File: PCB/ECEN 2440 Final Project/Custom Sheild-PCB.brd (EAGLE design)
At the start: 100 x 80 mm, 4 parts

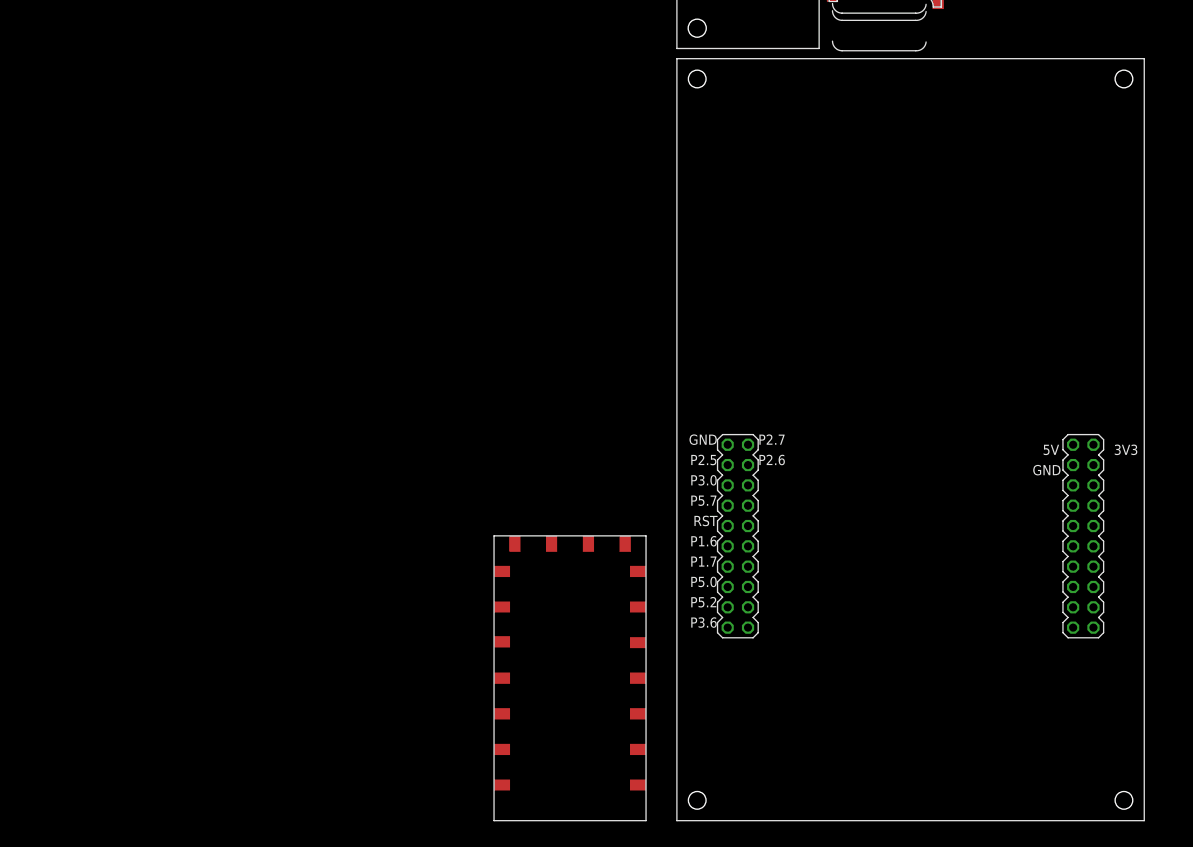
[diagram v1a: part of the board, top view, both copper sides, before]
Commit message: made a couple connections
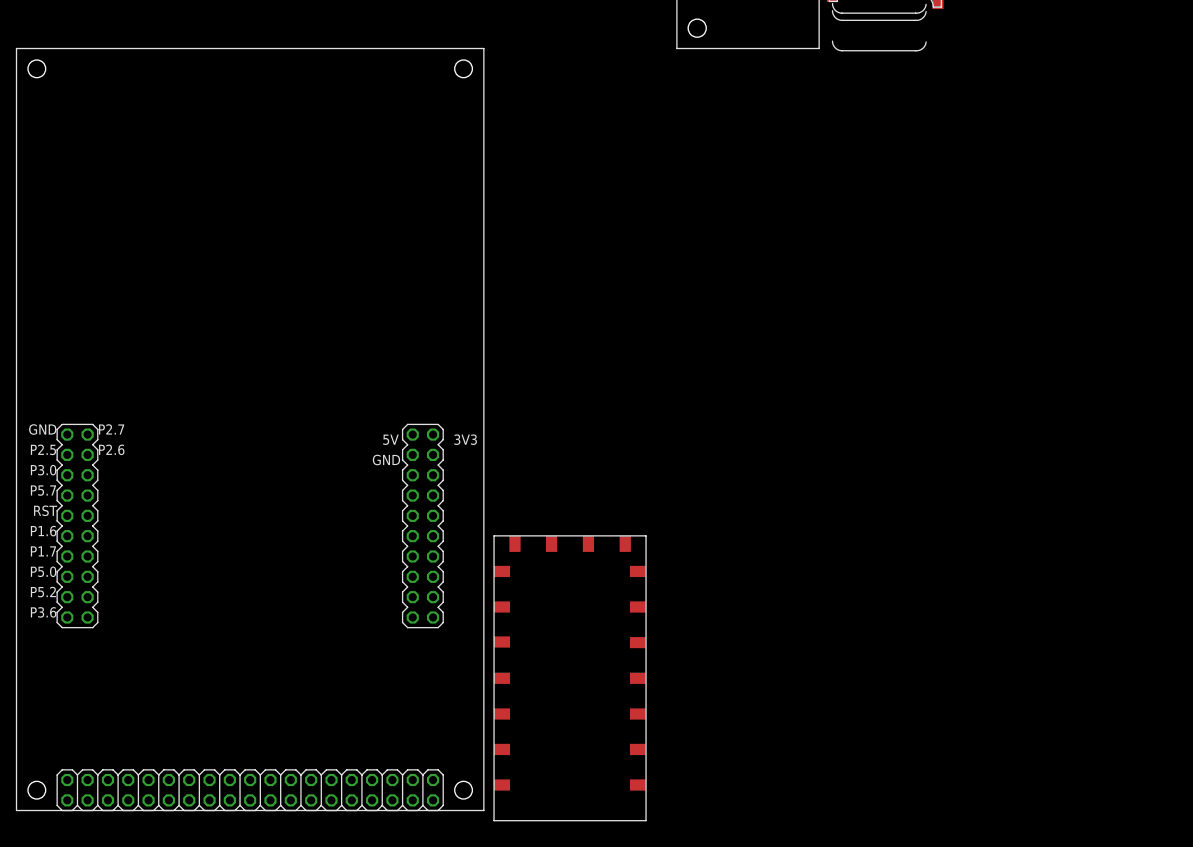
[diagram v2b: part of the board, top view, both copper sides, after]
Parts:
- moved U$3 82.6 mm to (-154.9, 2.54)
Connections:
- new net 1: U$3.GND1
- new net 29: U$3.GND2
- net GND1: no longer U$3.GND1, U$3.GND2
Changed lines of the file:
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@@
 <attribute name="NAME" x="-74.3712" y="114.3762" size="1.27" layer="25" ratio="10" rot="R270"/>
 </element>
-<element name="U$3" library="Custom Library" package="MSP432" value="MSP432" x="-72.39" y="1.27" smashed="yes"/>
 <element name="U$4" library="Custom Library" package="RADIO" value="RADIO" x="-95.25" y="1.27" smashed="yes"/>
+<element name="U$3" library="Custom Library" package="MSP432" value="MSP432" x="-154.94" y="2.54" smashed="yes">
+<attribute name="VALUE" x="-149.86" y="0.635" size="1.27" layer="27"/>
+</element>
 </elements>
 <signals>
-<signal name="30">
-<contactref element="U$3" pad="5V"/>
-</signal>
 <signal name="GND1">
-<contactref element="U$3" pad="GND1"/>
 <contactref element="U$2" pad="GND"/>
 <contactref element="U$1" pad="MT1"/>
@@
 <contactref element="U$4" pad="GND1"/>
 <contactref element="U$4" pad="GND"/>
-<contactref element="U$3" pad="GND2"/>
 <wire x1="-52.94" y1="104.57" x2="-39.74" y2="103.67" width="0" layer="19" extent="1-1"/>
 <wire x1="-69.85" y1="105.41" x2="-52.94" y2="104.57" width="0" layer="19" extent="1-1"/>
-<wire x1="-66.04" y1="48.26" x2="-69.85" y2="105.41" width="0" layer="19" extent="1-1"/>
-<wire x1="-83.45" y1="35.87" x2="-66.04" y2="48.26" width="0" layer="19" extent="1-1"/>
+<wire x1="-83.45" y1="35.87" x2="-69.85" y2="105.41" width="0" layer="19" extent="1-1"/>
 <wire x1="-88.05" y1="35.87" x2="-83.45" y2="35.87" width="0" layer="19" extent="1-1"/>
-<wire x1="-22.86" y1="45.72" x2="-66.04" y2="48.26" width="0" layer="19" extent="1-1"/>
 </signal>
 <signal name="N$1">
+<contactref element="U$2" pad="SDA"/>
 <contactref element="U$3" pad="P1.6"/>
-<contactref element="U$2" pad="SDA"/>
-<wire x1="-66.04" y1="35.56" x2="-69.85" y2="107.95" width="0" layer="19" extent="1-1"/>
+<wire x1="-69.85" y1="107.95" x2="-148.59" y2="36.83" width="0" layer="19" extent="1-1"/>
 </signal>
 <signal name="N$2">
+<contactref element="U$2" pad="SCL"/>
 <contactref element="U$3" pad="P1.7"/>
-<contactref element="U$2" pad="SCL"/>
-<wire x1="-66.04" y1="33.02" x2="-69.85" y2="110.49" width="0" layer="19" extent="1-1"/>
+<wire x1="-69.85" y1="110.49" x2="-148.59" y2="34.29" width="0" layer="19" extent="1-1"/>
 </signal>
 <signal name="N$3">
-<contactref element="U$3" pad="3V3"/>
 <contactref element="U$4" pad="VBAT"/>
 <contactref element="U$2" pad="3V3"/>
-<wire x1="-20.32" y1="48.26" x2="-92.65" y2="35.87" width="0" layer="19" extent="1-1"/>
-<wire x1="-69.85" y1="113.03" x2="-92.65" y2="35.87" width="0" layer="19" extent="1-1"/>
+<contactref element="U$3" pad="3V3"/>
+<wire x1="-102.87" y1="49.53" x2="-92.65" y2="35.87" width="0" layer="19" extent="1-1"/>
+<wire x1="-69.85" y1="113.03" x2="-102.87" y2="49.53" width="0" layer="19" extent="1-1"/>
 </signal>
 <signal name="RX_RADIO">
 <contactref element="U$4" pad="RXD"/>
 <contactref element="U$3" pad="P3.3"/>
-<wire x1="-20.32" y1="40.64" x2="-77.25" y2="14.62" width="0" layer="19" extent="1-1"/>
+<wire x1="-102.87" y1="41.91" x2="-77.25" y2="14.62" width="0" layer="19" extent="1-1"/>
 </signal>
 <signal name="TX_RADIO">
 <contactref element="U$4" pad="TXD"/>
 <contactref element="U$3" pad="P3.2"/>
-<wire x1="-20.32" y1="43.18" x2="-77.25" y2="10.17" width="0" layer="19" extent="1-1"/>
+<wire x1="-102.87" y1="44.45" x2="-77.25" y2="10.17" width="0" layer="19" extent="1-1"/>
 </signal>
 <signal name="N$4">
@@
 <contactref element="U$1" pad="5"/>
 </signal>
+<signal name="1">
+<contactref element="U$3" pad="GND1"/>
+</signal>
+<signal name="29">
+<contactref element="U$3" pad="GND2"/>
+</signal>
+<signal name="30">
+<contactref element="U$3" pad="5V"/>
+</signal>
 </signals>

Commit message: PDR schematic and board
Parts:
- added BATTERY: (no value), pinhead:1X02
- added C1, C2, C3: (no value), rcl:C0805
- added R1, R2, R3: (no value), rcl:R0805
- added SJ1, SJ2: (no value), jumper:SJ_2W
- added TEENSY: (no value), pinhead:1X04
- added U$6: LFCN-160+, Custom Library:LFCN-160+
- added U1: V_REG_NCP50X, SparkFun-IC-Power:DPAK-5
- added X1: (no value), adafruit:SMA_EDGELAUNCH
- moved U$3 156.2 mm to (1.27, 1.27)
- moved U$4 150.0 mm to (40.6, 64.8), turned to 90 degrees
- moved U$1 142.9 mm to (52.1, 21.6), turned to 270 degrees
- moved U$2 113.5 mm to (19.1, 30.5)
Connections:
- net N$1 renamed ALT_SDA
- net N$2 renamed ALT_SCL
- removed net 1: U$3.GND1
- removed net GND1: U$1.MT1, U$1.MT2, U$2.GND, U$4.GND, U$4.GND1
- new net +3V3: SJ2.2, TEENSY.4, U$1.4, U$2.3V3, U$3.3V3, U$4.VBAT
- new net AUDIO_PTT: U$3.P2.3, U$4.PTT
- new net AUDIO_PWM: R1.1, U$3.P2.4
- new net CD1: U$1.CD1, U$3.10.4
- new net GND: C1.2, C2.2, C3.2, TEENSY.1, U$1.6, U$1.MT1, U$1.MT2, U$2.GND, U$3.GND1, U$3.GND10, U$3.GND11, U$4.GND, U$4.GND1, U$6.GND1, U$6.GND2, U$6.P$1, U$6.P$2, X1.GND@1, X1.GND@2, X1.GND@3, X1.GND@4
- new net N$1: U$4.ANT, U$6.RF-IN
- new net N$2: C1.1, R1.2, R2.1
- new net N$6: U$6.RF-OUT, X1.P
- new net N$7: SJ1.1, U1.VIN
- new net N$8: SJ2.3, U1.VOUT
- new net SD_CLK: U$1.5, U$3.10.1
- new net SD_CS_SPI: U$1.2, U$3.10.0
- new net SD_MISO: U$1.7, U$3.10.2
- new net SD_MOSI: U$1.3, U$3.10.3
- new net TEENSY_RX: TEENSY.2, U$3.9.7
- new net TEENSY_TX: TEENSY.3, U$3.9.6
- new net VCC: BATTERY.2, SJ1.2
- new net VSS: BATTERY.1
- net N$3: now also U$1.CD2; no longer U$2.3V3, U$3.3V3, U$4.VBAT
- net N$4: now also C2.1, R2.2, R3.1; no longer U$1.2
- net N$5: now also C3.1, R3.2, U$4.MIC_IN; no longer U$1.5
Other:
- board size 100 x 80 mm -> 63.2 x 97.8 mm
- board text added: "LONG-SIDE PINS"
- board text added: "SHORT-SIDE PINS"

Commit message: Final board and schematic
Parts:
- added SD_BREAKOUT: (no value), pinhead:1X07
- moved BATTERY 52.1 mm to (57.1, 10.2)
- moved SJ1 48.5 mm to (57.1, 17.8)
- moved TEENSY 35.6 mm to (21.6, 15.2), turned to 270 degrees
- moved U1 33.1 mm to (48.3, 11.4), turned to 270 degrees
- moved U$1 33.0 mm to (19.1, 21.6)
- moved SJ2 12.8 mm to (35.6, 12.7)
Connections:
- removed net N$3: U$1.CD2
- net +3V3: now also SD_BREAKOUT.6
- net CD1: now also SD_BREAKOUT.1
- net GND: now also SD_BREAKOUT.7
- net SD_CLK: now also SD_BREAKOUT.4
- net SD_CS_SPI: now also SD_BREAKOUT.5
- net SD_MISO: now also SD_BREAKOUT.2
- net SD_MOSI: now also SD_BREAKOUT.3

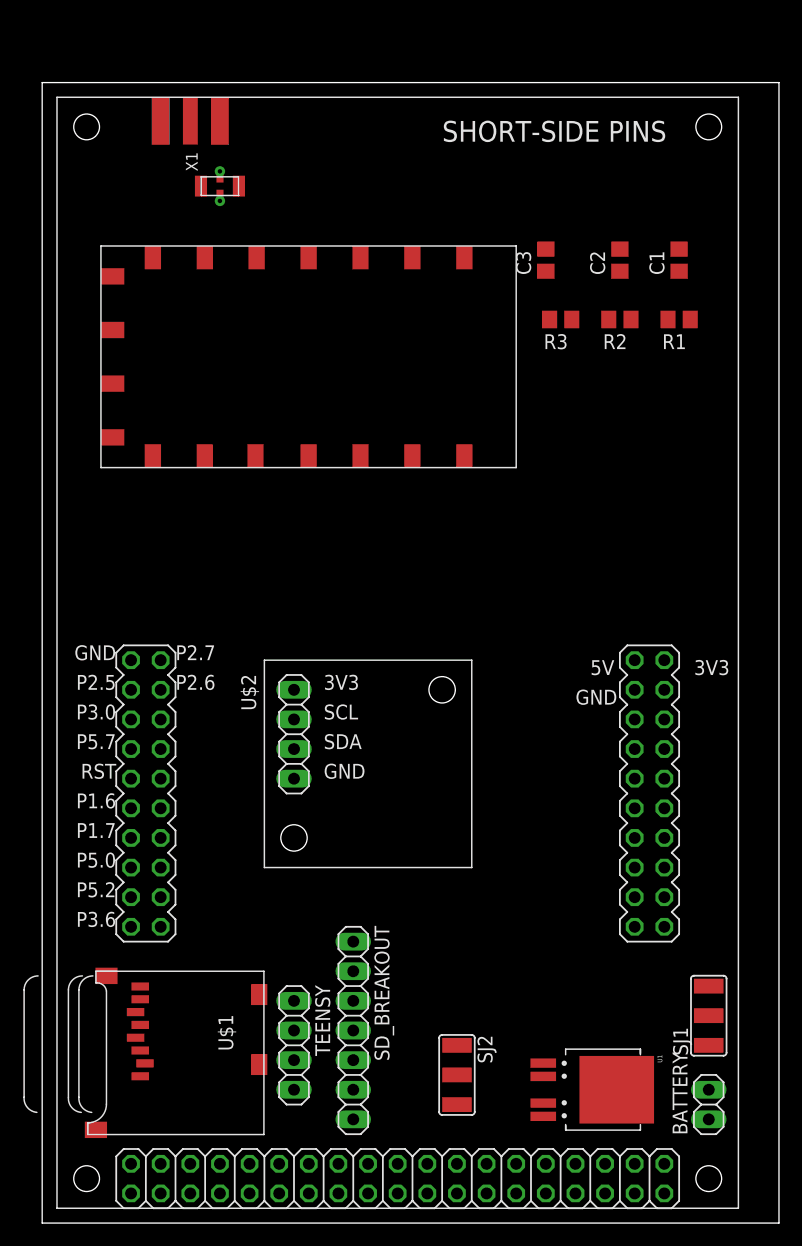
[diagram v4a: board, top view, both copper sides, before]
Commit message: Made updates to board and created now radio breakout board
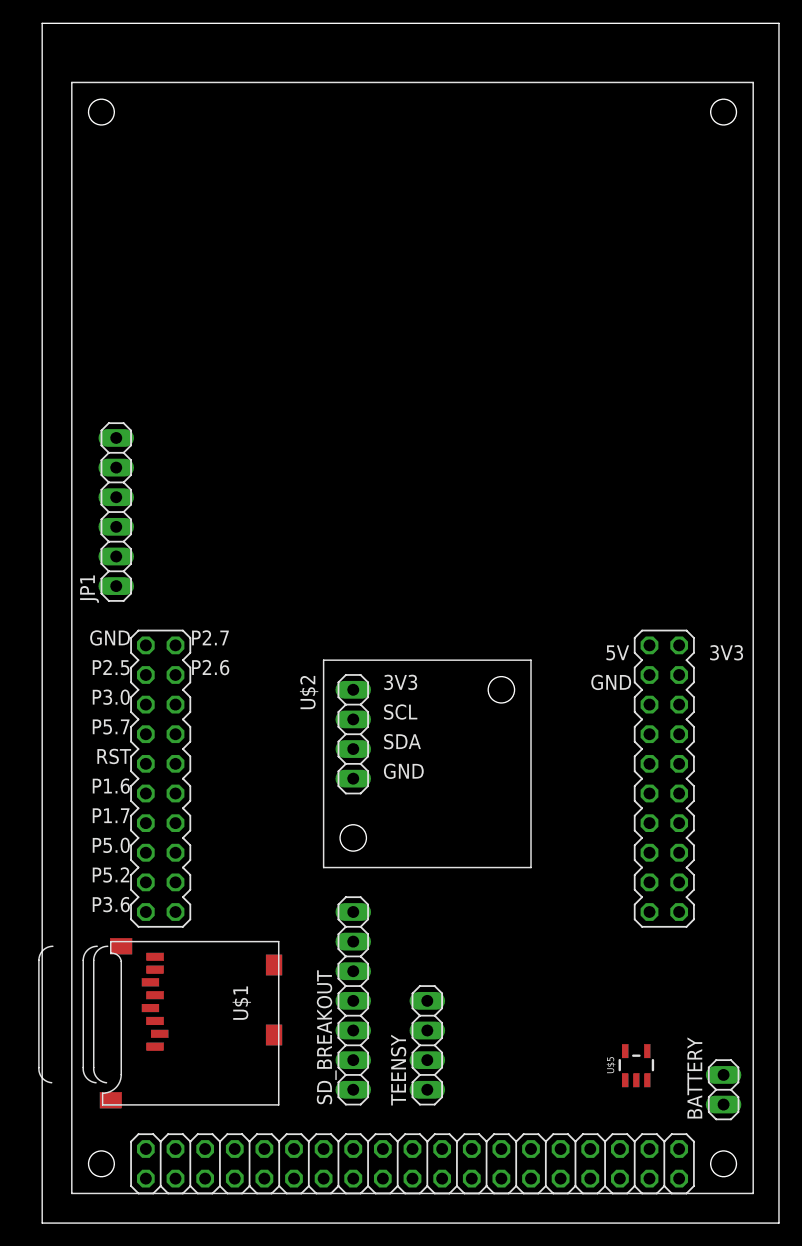
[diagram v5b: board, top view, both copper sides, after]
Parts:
- removed C1, C2, C3: (no value), rcl:C0805
- removed R1, R2, R3: (no value), rcl:R0805
- removed SJ1, SJ2: (no value), jumper:SJ_2W
- removed U$4: RADIO, Custom Library:RADIO
- removed U$6: LFCN-160+, Custom Library:LFCN-160+
- removed U1: V_REG_NCP50X, SparkFun-IC-Power:DPAK-5
- removed X1: (no value), adafruit:SMA_EDGELAUNCH
- added JP1: (no value), pinhead:1X06
- added U$5: LDO-S-816, Custom Library:LDO-S-816
- moved TEENSY 11.4 mm to (33.0, 15.2), turned to 90 degrees
- moved U$2 5.08 mm to (24.1, 30.5)
- moved U$1 2.84 mm to (20.3, 24.1)
- moved SD_BREAKOUT 2.54 mm to (26.7, 19.1), turned to 90 degrees
- moved BATTERY 1.80 mm to (58.4, 11.4)
- moved U$3 1.80 mm to (2.54, 2.54)
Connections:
- removed net 29: U$3.GND2
- removed net 30: U$3.5V
- removed net N$1: U$4.ANT, U$6.RF-IN
- removed net N$2: C1.1, R1.2, R2.1
- removed net N$4: C2.1, R2.2, R3.1
- removed net N$5: C3.1, R3.2, U$4.MIC_IN
- removed net N$6: U$6.RF-OUT, X1.P
- removed net N$7: SJ1.1, U1.VIN
- removed net N$8: SJ2.3, U1.VOUT
- removed net VSS: BATTERY.1
- net +3V3: now also JP1.6; no longer SJ2.2, U$4.VBAT
- net AUDIO_PTT: now also JP1.4; no longer U$4.PTT
- net AUDIO_PWM: now also JP1.3; no longer R1.1
- net GND: now also BATTERY.1, JP1.5, U$3.GND2, U$5.VSS; no longer C1.2, C2.2, C3.2, U$4.GND, U$4.GND1, U$6.GND1, U$6.GND2, U$6.P$1, U$6.P$2, X1.GND@1, X1.GND@2, X1.GND@3, X1.GND@4
- net RX_RADIO: now also JP1.2; no longer U$4.RXD
- net TX_RADIO: now also JP1.1; no longer U$4.TXD
- net VCC: now also U$3.5V, U$3.5VA, U$3.5VB, U$5.VIN; no longer SJ1.2
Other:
- board size 63.2 x 97.8 mm -> 63.2 x 102.9 mm
- board text removed: "LONG-SIDE PINS"
- board text removed: "SHORT-SIDE PINS"

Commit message: minor changes to board
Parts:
- removed U$5: LDO-S-816, Custom Library:LDO-S-816
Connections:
- net GND: no longer U$5.VSS
- net VCC: no longer U$5.VIN
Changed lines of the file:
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@@
 <attribute name="VALUE" x="8.89" y="0.635" size="1.27" layer="27"/>
-</element>
-<element name="U$5" library="Custom Library" package="LDO-S-816" value="LDO-S-816" x="49.53" y="12.7" smashed="yes">
-<attribute name="NAME" x="49.035" y="13.54" size="0.6096" layer="25" font="vector" ratio="20" rot="R90" align="bottom-center"/>
-<attribute name="VALUE" x="53.48" y="14.81" size="0.6096" layer="27" font="vector" ratio="20" rot="R90" align="bottom-center"/>
 </element>
 <element name="JP1" library="pinhead" library_urn="urn:adsk.eagle:library:325" package="1X06" package3d_urn="urn:adsk.eagle:package:22472/2" value="" x="6.35" y="60.96" smashed="yes" rot="R90">
@@
 <contactref element="SD_BREAKOUT" pad="7"/>
 <contactref element="BATTERY" pad="1"/>
-<contactref element="U$5" pad="VSS"/>
 <contactref element="U$3" pad="GND2"/>
 <contactref element="JP1" pad="5"/>
@@
 <wire x1="26.67" y1="26.67" x2="26.67" y2="38.1" width="0" layer="19" extent="1-1"/>
 <wire x1="33.02" y1="11.43" x2="26.67" y2="26.67" width="0" layer="19" extent="1-1"/>
-<wire x1="50.94" y1="12.2399" x2="33.02" y2="11.43" width="0" layer="19" extent="1-1"/>
-<wire x1="58.42" y1="10.16" x2="50.94" y2="12.2399" width="0" layer="19" extent="1-1"/>
 <wire x1="9.28" y1="20.63" x2="26.67" y2="26.67" width="0" layer="19" extent="1-1"/>
 <wire x1="6.78" y1="23.73" x2="9.28" y2="20.63" width="0" layer="19" extent="1-1"/>
@@
 <wire x1="8.89" y1="49.53" x2="26.67" y2="38.1" width="0" layer="19" extent="1-1"/>
 <wire x1="6.35" y1="64.77" x2="8.89" y2="49.53" width="0" layer="19" extent="1-1"/>
+<wire x1="58.42" y1="10.16" x2="33.02" y2="11.43" width="0" layer="19" extent="1-1"/>
 </signal>
 <signal name="ALT_SDA">
@@
 <signal name="VCC">
 <contactref element="BATTERY" pad="2"/>
-<contactref element="U$5" pad="VIN"/>
 <contactref element="U$3" pad="5V"/>
 <contactref element="U$3" pad="5VA"/>
 <contactref element="U$3" pad="5VB"/>
-<wire x1="51.89" y1="14.7401" x2="52.07" y2="49.53" width="0" layer="19" extent="1-1"/>
-<wire x1="58.42" y1="12.7" x2="51.89" y2="14.7401" width="0" layer="19" extent="1-1"/>
-<wire x1="13.97" y1="6.35" x2="51.89" y2="14.7401" width="0" layer="19" extent="1-1"/>
+<wire x1="58.42" y1="12.7" x2="52.07" y2="49.53" width="0" layer="19" extent="1-1"/>
+<wire x1="13.97" y1="6.35" x2="58.42" y2="12.7" width="0" layer="19" extent="1-1"/>
 <wire x1="13.97" y1="3.81" x2="13.97" y2="6.35" width="0" layer="19" extent="1-1"/>
 </signal>

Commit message: New changes to pcb board
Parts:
- added R1, R2: 2.2k, SparkFun-Resistors:0603
- added SJ1: (no value), jumper:SJ_2
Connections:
- new net N$1: R1.2, SJ1.3
- new net N$2: R2.2, SJ1.1
- net +3V3: now also SJ1.2
- net ALT_SCL: now also R2.1
- net ALT_SDA: now also R1.1
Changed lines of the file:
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@@
 <attribute name="VALUE" x="9.525" y="53.34" size="1.27" layer="27" rot="R90"/>
+</element>
+<element name="SJ1" library="jumper" library_urn="urn:adsk.eagle:library:252" package="SJ_2" package3d_urn="urn:adsk.eagle:package:15474/1" value="" x="3.81" y="-3.81" smashed="yes">
+<attribute name="NAME" x="1.397" y="-2.54" size="1.27" layer="25" ratio="10"/>
+<attribute name="POPULARITY" value="7" x="3.81" y="-3.81" size="1.778" layer="27" display="off"/>
+<attribute name="VALUE" x="3.7099" y="-3.81" size="0.02" layer="27"/>
+</element>
+<element name="R1" library="SparkFun-Resistors" library_urn="urn:adsk.eagle:library:532" package="0603" package3d_urn="urn:adsk.eagle:package:39650/1" value="2.2k" x="2.54" y="-7.62" smashed="yes">
+<attribute name="NAME" x="2.54" y="-6.858" size="0.6096" layer="25" font="vector" ratio="20" align="bottom-center"/>
+<attribute name="PROD_ID" value="RES-08272" x="2.54" y="-7.62" size="1.778" layer="27" display="off"/>
+<attribute name="VALUE" x="2.54" y="-8.382" size="0.6096" layer="27" font="vector" ratio="20" align="top-center"/>
+</element>
+<element name="R2" library="SparkFun-Resistors" library_urn="urn:adsk.eagle:library:532" package="0603" package3d_urn="urn:adsk.eagle:package:39650/1" value="2.2k" x="2.54" y="-11.43" smashed="yes">
+<attribute name="NAME" x="2.54" y="-10.668" size="0.6096" layer="25" font="vector" ratio="20" align="bottom-center"/>
+<attribute name="PROD_ID" value="RES-08272" x="2.54" y="-11.43" size="1.778" layer="27" display="off"/>
+<attribute name="VALUE" x="2.54" y="-12.192" size="0.6096" layer="27" font="vector" ratio="20" align="top-center"/>
 </element>
 </elements>
@@
 <contactref element="U$2" pad="SDA"/>
 <contactref element="U$3" pad="P1.6"/>
+<contactref element="R1" pad="1"/>
 <wire x1="8.89" y1="36.83" x2="26.67" y2="40.64" width="0" layer="19" extent="1-1"/>
+<wire x1="1.69" y1="-7.62" x2="8.89" y2="36.83" width="0" layer="19" extent="1-1"/>
 </signal>
 <signal name="ALT_SCL">
 <contactref element="U$2" pad="SCL"/>
 <contactref element="U$3" pad="P1.7"/>
+<contactref element="R2" pad="1"/>
 <wire x1="8.89" y1="34.29" x2="26.67" y2="43.18" width="0" layer="19" extent="1-1"/>
+<wire x1="1.69" y1="-11.43" x2="8.89" y2="34.29" width="0" layer="19" extent="1-1"/>
 </signal>
 <signal name="RX_RADIO">
@@
 <contactref element="SD_BREAKOUT" pad="6"/>
 <contactref element="JP1" pad="6"/>
+<contactref element="SJ1" pad="2"/>
 <wire x1="26.67" y1="45.72" x2="54.61" y2="49.53" width="0" layer="19" extent="1-1"/>
 <wire x1="26.67" y1="24.13" x2="26.67" y2="45.72" width="0" layer="19" extent="1-1"/>
 <wire x1="33.02" y1="19.05" x2="26.67" y2="24.13" width="0" layer="19" extent="1-1"/>
 <wire x1="9.28" y1="18.43" x2="26.67" y2="24.13" width="0" layer="19" extent="1-1"/>
+<wire x1="3.81" y1="-3.81" x2="9.28" y2="18.43" width="0" layer="19" extent="1-1"/>
 <wire x1="6.35" y1="67.31" x2="26.67" y2="45.72" width="0" layer="19" extent="1-1"/>
 </signal>
@@
 <wire x1="13.97" y1="3.81" x2="13.97" y2="6.35" width="0" layer="19" extent="1-1"/>
 </signal>
+<signal name="N$1">
+<contactref element="R1" pad="2"/>
+<contactref element="SJ1" pad="3"/>
+<wire x1="5.334" y1="-3.81" x2="3.39" y2="-7.62" width="0" layer="19" extent="1-1"/>
+</signal>
+<signal name="N$2">
+<contactref element="SJ1" pad="1"/>
+<contactref element="R2" pad="2"/>
+<wire x1="2.286" y1="-3.81" x2="3.39" y2="-11.43" width="0" layer="19" extent="1-1"/>
+</signal>
 </signals>

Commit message: Final updates to the board
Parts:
- moved R2 54.4 mm to (35.6, 31.8), turned to 270 degrees
- moved R1 47.6 mm to (29.2, 31.8), turned to 270 degrees
- moved SJ1 41.0 mm to (24.1, 31.8), turned to 90 degrees
- moved TEENSY 12.7 mm to (45.7, 15.2)
- moved JP1 7.18 mm to (11.4, 55.9), turned to 180 degrees
- moved U$2 6.48 mm to (22.9, 36.8)
- moved SD_BREAKOUT 5.08 mm to (31.8, 19.1)
